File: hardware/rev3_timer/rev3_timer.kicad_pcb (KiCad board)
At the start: 2 copper layers, 114.3 x 160 mm, 72 parts, among them J1 Conn_01x06, J2 Conn_02x03_Odd_Even, J3 Conn_01x06, J4 Conn_01x02, SW1 SW_Push, SW2 SW_Push, SW3 SW_Push, SW4 SW_Push, U1 ATmega168-20P, U10 SN75468, U11 IN-12A/B, U12 IN-12A/B, U13 IN-12A/B, U14 IN-12A/B, U15 LM7805_TO220, U16 SN76489, U17 LM380N, U18 74HC164, U19 SN75468, U2 74HC164, U3 74HC164, U4 74HC164, U5 74HC164, U6 SN75468, U7 SN75468, U8 SN75468, U9 SN75468

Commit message: working on placement
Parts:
- added C17: 0.1uF, Capacitor_THT:C_Disc_D3.0mm_W1.6mm_P2.50mm, F.Cu at (125.7, 106.7)
- moved R8 16.4 mm to (123.2, 29.3)
- moved R18 6.35 mm to (142.2, 67.3)
- moved U11 6.35 mm to (127.0, 48.3)
- moved U14 6.35 mm to (58.4, 48.3)
- moved D4 6.35 mm to (137.2, 77.5)
- moved D6 5.08 mm to (40.6, 43.2)
- moved NE3 5.08 mm to (40.6, 53.3)
- moved C6 5.04 mm to (110.5, 106.7), turned to 180 degrees
- moved C5 5.04 mm to (95.2, 106.7), turned to 180 degrees
- moved C8 2.54 mm to (63.5, 106.7)
- moved R4 2.54 mm to (102.9, 29.2)
- moved R6 2.54 mm to (54.6, 29.2)
- moved SW3 1.71 mm to (104.0, 69.8)
- moved SW4 1.71 mm to (120.5, 69.8)
- moved R16 1.37 mm to (113.0, 78.8)
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
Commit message: working on two-board design
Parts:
- added H1: MountingHole, MountingHole:MountingHole_4.3mm_M4_Pad, F.Cu at (39.4, 24.1)
- added H2: MountingHole, MountingHole:MountingHole_4.3mm_M4_Pad, F.Cu at (143.5, 95.2)
- added H3: MountingHole, MountingHole:MountingHole_4.3mm_M4_Pad, F.Cu at (39.4, 174.0)
- added H4: MountingHole, MountingHole:MountingHole_4.3mm_M4_Pad, F.Cu at (143.5, 110.5)
- added H5: MountingHole, MountingHole:MountingHole_4.3mm_M4_Pad, F.Cu at (143.5, 174.0)
- added H6: MountingHole, MountingHole:MountingHole_4.3mm_M4_Pad, F.Cu at (39.4, 110.5)
- added H7: MountingHole, MountingHole:MountingHole_4.3mm_M4_Pad, F.Cu at (39.4, 95.2)
- added H8: MountingHole, MountingHole:MountingHole_4.3mm_M4_Pad, F.Cu at (143.5, 24.1)
- moved D6 78.9 mm to (45.1, 121.9), turned to 90 degrees
- moved R10 78.5 mm to (36.8, 141.0), turned to 90 degrees
- moved R18 73.6 mm to (97.4, 125.7), turned to 90 degrees
- moved R9 67.4 mm to (41.3, 141.0)
- moved NE3 66.2 mm to (38.7, 119.5), turned to 0 degrees
- moved SW1 52.7 mm to (61.0, 121.3)
- moved SW2 52.5 mm to (83.2, 121.0)
- moved SW4 51.8 mm to (130.3, 120.8)
- moved SW3 51.6 mm to (111.5, 120.9)
- moved R14 44.2 mm to (53.6, 116.2), turned to -90 degrees
- moved U19 43.8 mm to (36.8, 40.6)
- moved U6 43.4 mm to (138.4, 40.6)
- moved U2 43.1 mm to (138.4, 72.4)
- moved C17 42.0 mm to (143.5, 68.6)
- moved R15 41.5 mm to (75.2, 116.2), turned to -90 degrees
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
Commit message: playing with placement
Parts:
- added J5: Conn_01x10, Connector_PinHeader_2.54mm:PinHeader_2x05_P2.54mm_Vertical, F.Cu at (50.8, 108.0)
- added J6: Conn_01x10, Connector_PinHeader_2.54mm:PinHeader_2x05_P2.54mm_Vertical, F.Cu at (50.8, 100.3)
- added J7: Conn_01x04, Connector_PinHeader_2.54mm:PinHeader_1x04_P2.54mm_Vertical, F.Cu at (108.0, 106.7)
- added J8: Conn_01x04, Connector_PinHeader_2.54mm:PinHeader_1x04_P2.54mm_Vertical, F.Cu at (108.0, 99.1)
- moved J1 31.4 mm to (54.6, 181.6), turned to 90 degrees
- moved H3 7.62 mm to (39.4, 181.6)
- moved H5 7.62 mm to (143.5, 181.6)
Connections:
- U1 pad 14: /display/SR_nRST -> Net-(U1-Pad14)
- U1 pad 15: /display/SR_CLK -> Net-(U1-Pad15)
- U1 pad 16: /display/SR_DATA -> Net-(U1-Pad16)
- U1 pad 5: /display/NE_CTL -> Net-(U1-Pad5)
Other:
- board size 114.3 x 160 mm -> 114.3 x 167.6 mm

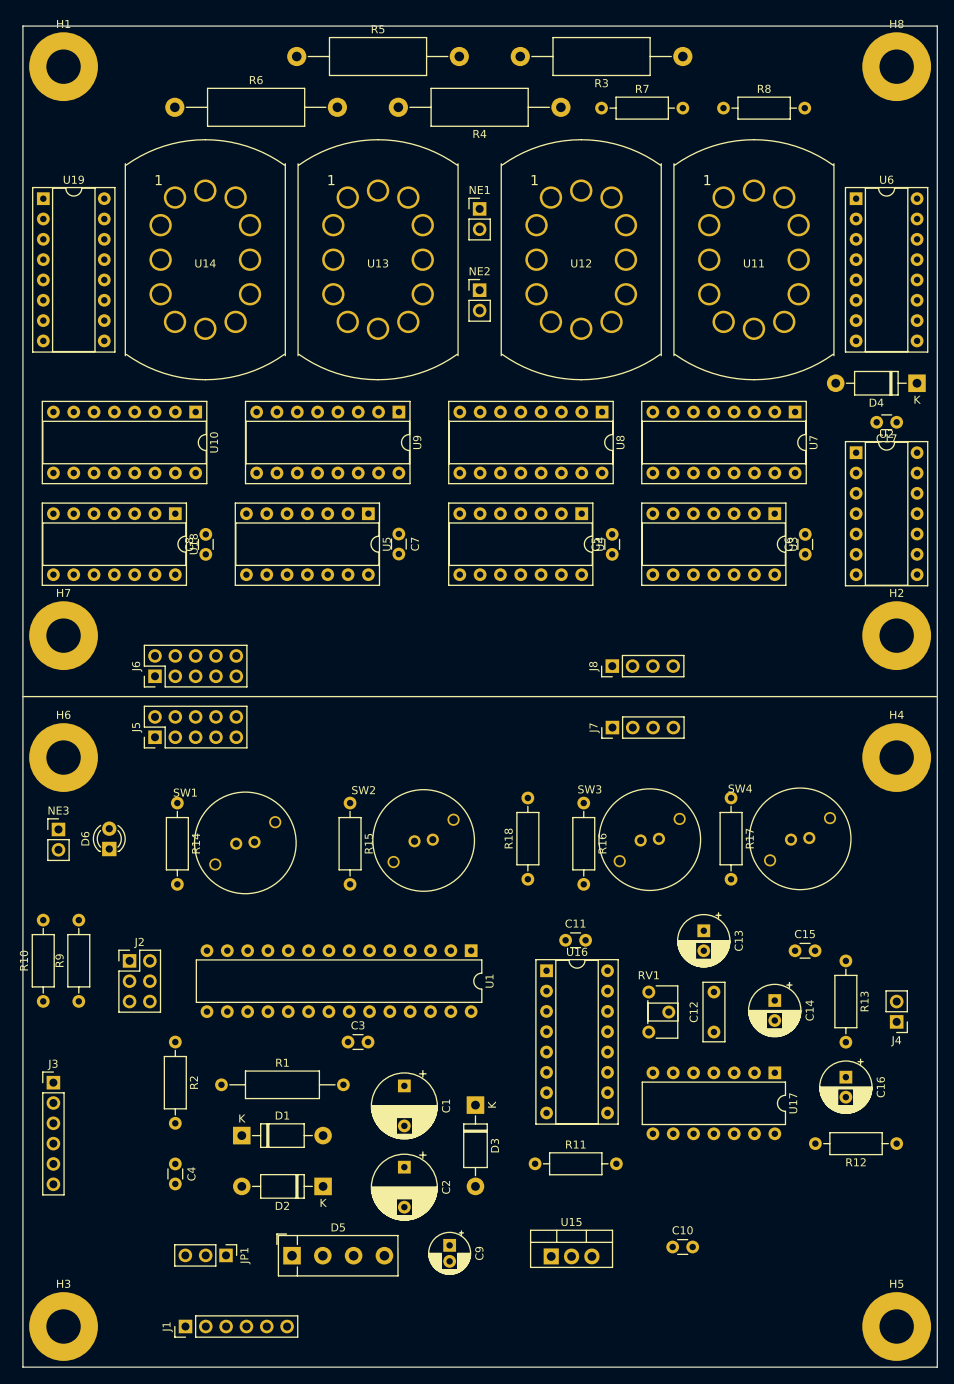
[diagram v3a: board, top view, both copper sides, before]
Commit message: add RTC, rearrange placement
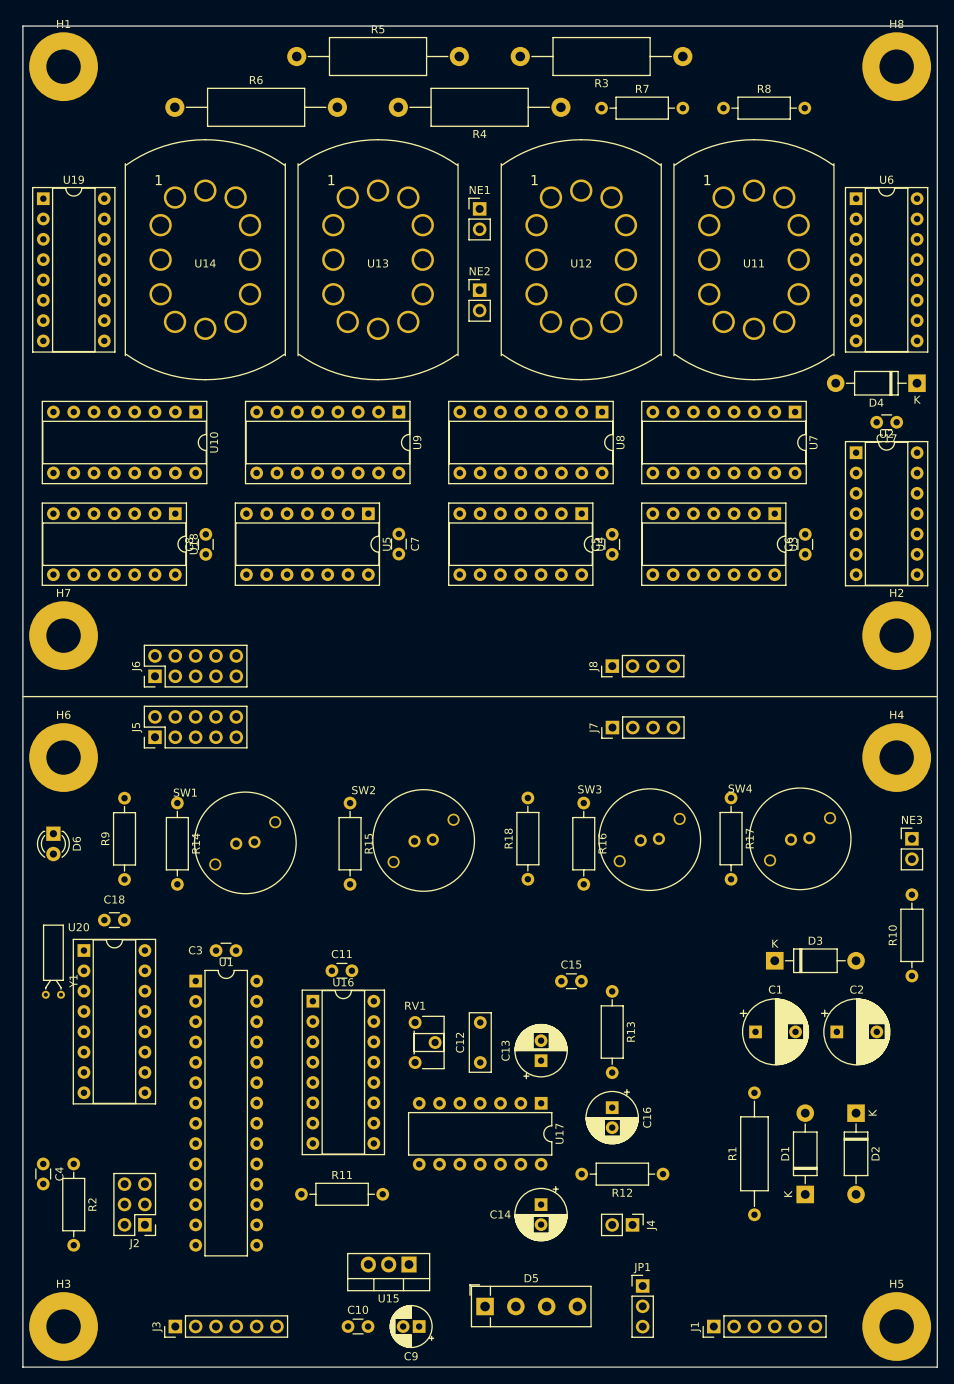
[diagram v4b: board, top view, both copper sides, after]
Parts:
- added C18: 0.1uF, Capacitor_THT:C_Disc_D3.0mm_W1.6mm_P2.50mm, F.Cu at (47.0, 130.8)
- added U20: DS1306, Package_DIP:DIP-16_W7.62mm_Socket, F.Cu at (41.9, 134.6)
- added Y1: Crystal_Small, Crystal:Crystal_C26-LF_D2.1mm_L6.5mm_Horizontal, F.Cu at (39.0, 140.1)
- moved R10 108.6 mm to (145.4, 137.8)
- moved NE3 106.7 mm to (145.4, 120.7)
- moved D1 70.8 mm to (132.1, 165.1), turned to 90 degrees
- moved R1 68.6 mm to (125.7, 167.6), turned to 90 degrees
- moved D2 67.2 mm to (138.4, 154.9), turned to -90 degrees
- moved J1 66.0 mm to (120.7, 181.6)
- moved C2 56.6 mm to (136.0, 144.8), turned to 0 degrees
- moved JP1 52.2 mm to (111.8, 176.5), turned to 0 degrees
- moved C1 44.4 mm to (125.9, 144.8), turned to 0 degrees
- moved C10 41.8 mm to (74.9, 181.6)
- moved J4 41.6 mm to (110.5, 168.9), turned to -90 degrees
- moved D3 41.5 mm to (128.3, 135.9), turned to 0 degrees
- moved C14 38.8 mm to (99.1, 166.4)
- moved U1 34.6 mm to (55.9, 138.4), turned to 0 degrees
- moved J3 34.1 mm to (53.3, 181.6), turned to 90 degrees
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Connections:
- U1 pad 11: unconnected-(U1-Pad11) -> /RTC_CE
